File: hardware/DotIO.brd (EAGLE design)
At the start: 30 x 65 mm, 37 parts, among them CN1 1X4-BIG, U1 ATMEGA328P-MU-QFN32, X1 S4B-ZR, X2 S4B-ZR, X3 S4B-ZR, X4 S4B-ZR, X5 S4B-ZR, X6 S4B-ZR, X7 S4B-ZR

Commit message: Initial routing
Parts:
- removed LED5, LED6, LED7, LED8: (no value), SparkFun:LED-0603
- removed X2: S4B-ZR, con-jst:S4B-ZR
- added C1, C9: 1uF, rcl:C0603
- added D1, D2: (no value), diode:SOD523
- added IC2: (no value), MCP1700:SOT-23
- added J3: USB-MICROB, SparkFun-Retired:USB-MICROB
- added R6: 68Ω, rcl:R0603
- added R8: 1.5kΩ, rcl:R0603
- R2: value 150Ω -> 68Ω; device SparkFun:0603-ARV -> rcl:R0603
- moved CN1 67.2 mm to (9.30, 28.0), turned to 0 degrees
- moved R2 47.5 mm to (8.12, 7.39), turned to 0 degrees
- moved LED2 45.9 mm to (2.06, 48.1), turned to 180 degrees
- moved LOGO1 17.0 mm to (2.50, 28.8), turned to 90 degrees
- moved R7 16.2 mm to (2.37, 17.3)
- moved C2 13.8 mm to (2.73, 52.8), turned to 270 degrees
- moved R4 11.2 mm to (21.4, 54.1), turned to 270 degrees
- moved U1 4.90 mm to (13.5, 16.2)
- moved Y1 4.76 mm to (14.7, 10.9)
- moved X1 1.62 mm to (5.06, 60.6), flipped to the bottom, turned to 90 degrees
- moved R3 1.10 mm to (20.9, 28.1)
- moved LED3 0.59 mm to (21.0, 41.7)
- moved LED4 0.53 mm to (21.0, 39.6)
- moved LED12 0.43 mm to (20.9, 31.8)
- moved LED11 0.42 mm to (20.9, 34.2)
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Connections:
- net LED renamed RGB_RED
- removed net ADCENA: U1.13
- removed net CS_FLASH: U1.23
- removed net N$11: LED6.C, R2.1
- removed net N$12: LED7.C, R2.2
- removed net N$13: LED8.C, R2.4
- removed net N$3: LED5.C, R2.3
- removed net OUTA: LED11.A, LED3.A, LED5.A, LED6.A, U1.14, X1.3, X2.3, X3.3, X5.3
- removed net OUTB: LED12.A, LED4.A, LED7.A, LED8.A, X1.2, X2.2, X3.2, X5.2
- removed net RSEL: U1.26
- removed net RXD: R1.3
- removed net TXD: R1.2
- new net 4_0: LED11.A, U1.23, X5.3
- new net 4_1: LED12.A, U1.24, X5.2
- new net 5_0: LED3.A, U1.25, X3.3
- new net 5_1: LED4.A, U1.26, X3.2
- new net RGB_BLUE: R1.3, U1.14
- new net RGB_GREEN: R1.2, U1.13
- new net USB_D+: D2.C, J3.D+, R2.1
- new net USB_D-: D1.C, J3.D-, R6.1, R8.1
- net +3V3: now also C1.1, IC2.2, R8.2, X1.3
- net +5V: now also C9.1, IC2.3, J3.VBUS; no longer X1.4, X2.4
- net D+: now also R2.2; no longer U1.25
- net D-: now also R6.2; no longer U1.24
- net GND: now also C1.2, C9.2, D1.A, D2.A, IC2.1, J3.GND, J3.MT1, J3.MT2, X1.4; no longer R2.5, R2.6, R2.7, R2.8, X1.1, X2.1
- net SCL: now also X1.2
- net SDA: now also X1.1
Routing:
- net +3V3: track 0.00 -> 162.6 mm, vias 0 -> 2
- net SCL: track 0.00 -> 72.6 mm, vias 0 -> 2
- net +5V: track 0.00 -> 70.9 mm, vias 0 -> 2
- net PUSH_RIGHT: track 0.00 -> 63.1 mm, vias 0 -> 2
- net SDA: track 0.00 -> 60.6 mm, vias 0 -> 3
- net RGB_RED: track 0.00 -> 55.2 mm, vias 0 -> 4
- net RGB_GREEN: track 0.00 -> 53.7 mm, vias 0 -> 2
- net RGB_BLUE: track 0.00 -> 49.6 mm, vias 0 -> 2
- net PUSH_UP: track 0.00 -> 48.4 mm, vias 0 -> 2
- net 5_0: track 0.00 -> 45.9 mm, vias 0 -> 2
- net 2_0: track 0.00 -> 45.0 mm
- net MOSI: track 0.00 -> 38.7 mm
- net MISO: track 0.00 -> 36.5 mm
- net SCK: track 0.00 -> 35.4 mm
- net 5_1: track 0.00 -> 34.8 mm, vias 0 -> 1
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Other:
- outline, holes or cut-outs redrawn

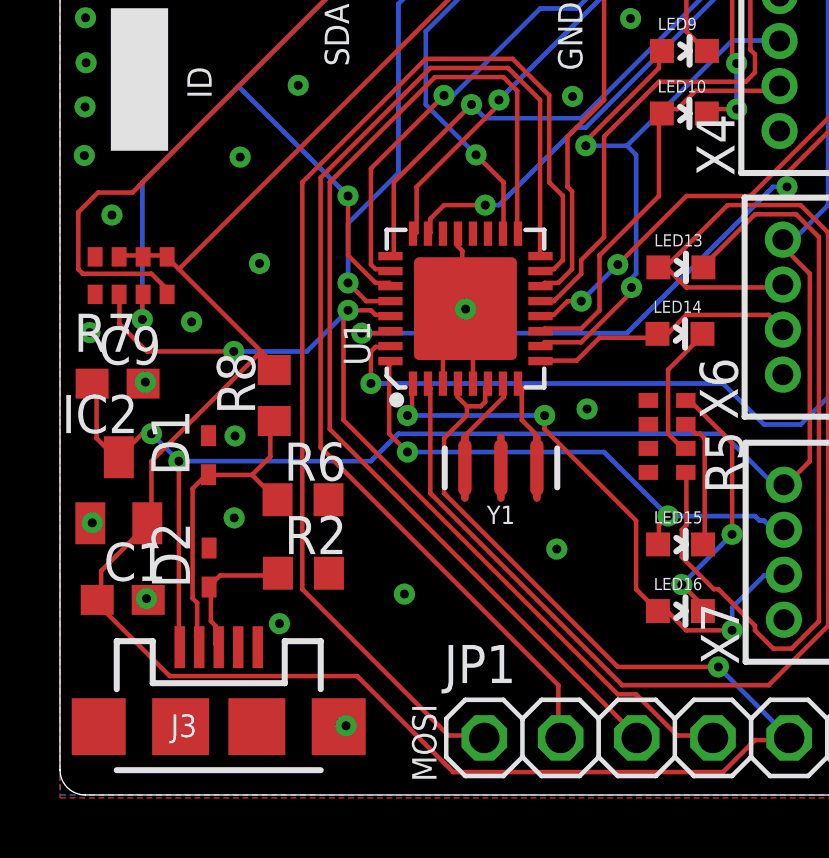
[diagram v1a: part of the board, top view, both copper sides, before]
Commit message: Bind USB to SPI pins
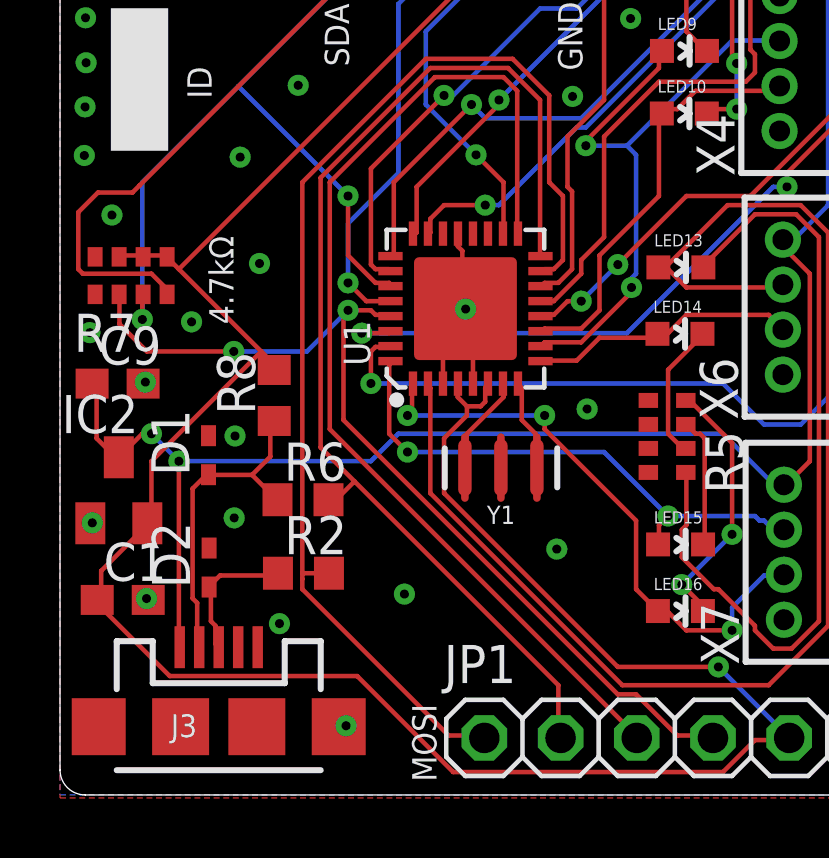
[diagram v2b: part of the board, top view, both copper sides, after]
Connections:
- removed net D+: R2.2
- removed net D-: R6.2
- net MISO: now also R6.2
- net MOSI: now also R2.2
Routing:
- net MISO: track 36.5 -> 37.6 mm
- net MOSI: track 38.7 -> 39.6 mm
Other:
- board text added: "4.7kΩ"
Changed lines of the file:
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@@
 <rectangle x1="10.73" y1="13.265" x2="16.46" y2="19.08" layer="43"/>
 <rectangle x1="0.905" y1="27.01" x2="4.305" y2="38.25" layer="43"/>
+<text x="5.785" y="15.69" size="0.8128" layer="21" rot="R90">4.7kΩ</text>
 </plain>
 <attributes>
@@
 <wire x1="12.192" y1="24.5364" x2="15.0876" y2="24.5364" width="0.1524" layer="1"/>
 <wire x1="8.0772" y1="20.4216" x2="12.192" y2="24.5364" width="0.1524" layer="1"/>
-<wire x1="8.0772" y1="6.858" x2="8.0772" y2="20.4216" width="0.1524" layer="1"/>
+<wire x1="8.0772" y1="6.858" x2="8.0772" y2="7.2" width="0.1524" layer="1"/>
+<wire x1="8.0772" y1="7.39" x2="8.0772" y2="20.4216" width="0.1524" layer="1"/>
 <wire x1="12.954" y1="1.9812" x2="8.0772" y2="6.858" width="0.1524" layer="1"/>
 <wire x1="14.0208" y1="1.9812" x2="12.954" y2="1.9812" width="0.1524" layer="1"/>
 <wire x1="16.1544" y1="17.526" x2="16.015" y2="17.46" width="0.1524" layer="1"/>
 <wire x1="14.0208" y1="1.9812" x2="14.145" y2="1.9" width="0.1524" layer="1"/>
+<contactref element="R2" pad="2"/>
+<wire x1="8.965" y1="7.39" x2="8.0772" y2="7.39" width="0.1524" layer="1"/>
+<wire x1="8.0772" y1="7.39" x2="8.0772" y2="7.2" width="0.1524" layer="1"/>
 </signal>
 <signal name="MISO">
@@
 <wire x1="8.6868" y1="20.574" x2="12.3444" y2="24.2316" width="0.1524" layer="1"/>
 <wire x1="8.6868" y1="11.5824" x2="8.6868" y2="20.574" width="0.1524" layer="1"/>
-<wire x1="16.6116" y1="3.6576" x2="8.6868" y2="11.5824" width="0.1524" layer="1"/>
+<wire x1="16.6116" y1="3.6576" x2="9.8171" y2="10.4521" width="0.1524" layer="1"/>
+<wire x1="9.8171" y1="10.4521" x2="8.6868" y2="11.5824" width="0.1524" layer="1"/>
 <wire x1="16.6116" y1="1.9812" x2="16.6116" y2="3.6576" width="0.1524" layer="1"/>
 <wire x1="16.002" y1="17.9832" x2="16.015" y2="17.96" width="0.1524" layer="1"/>
 <wire x1="16.6116" y1="1.9812" x2="16.685" y2="1.9" width="0.1524" layer="1"/>
+<contactref element="R6" pad="2"/>
+<wire x1="8.95" y1="9.84" x2="9.205" y2="9.84" width="0.1524" layer="1"/>
+<wire x1="9.205" y1="9.84" x2="9.8171" y2="10.4521" width="0.1524" layer="1"/>
 </signal>
 <signal name="SCK">
@@
 <wire x1="5.0292" y1="7.0104" x2="4.97" y2="6.93" width="0.1524" layer="1"/>
 </signal>
-<signal name="D-">
-<contactref element="R6" pad="2"/>
-</signal>
-<signal name="D+">
-<contactref element="R2" pad="2"/>
-</signal>
 <signal name="RGB_RED">

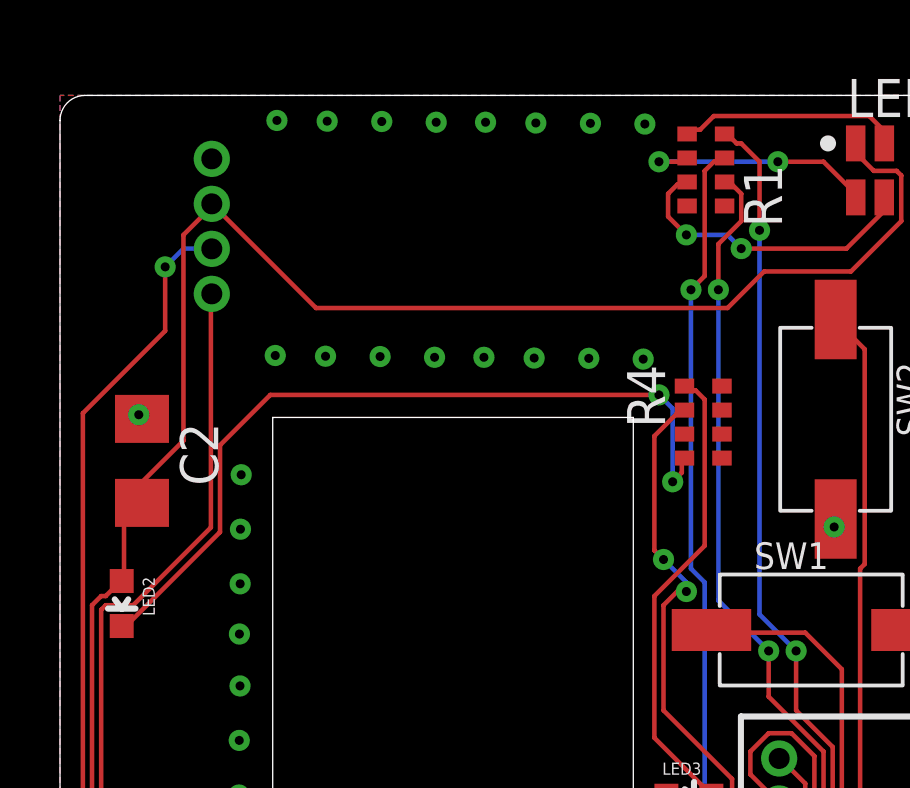
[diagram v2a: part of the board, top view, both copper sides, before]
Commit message: Flip I2C JST port
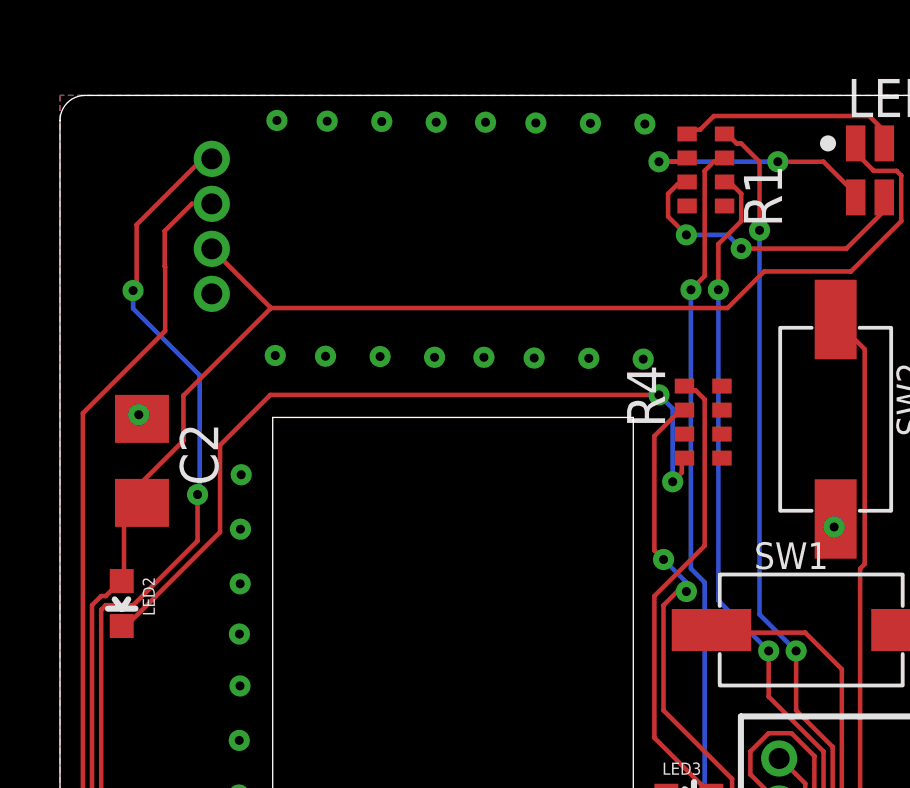
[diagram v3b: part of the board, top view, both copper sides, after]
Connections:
- net +3V3: now also X1.2; no longer X1.3
- net GND: now also X1.1; no longer X1.4
- net SCL: now also X1.3; no longer X1.2
- net SDA: now also X1.4; no longer X1.1
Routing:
- net SDA: track 60.6 -> 67.1 mm, vias 3 -> 5
- net +3V3: track 162.6 -> 159.3 mm
- net SCL: track 72.6 -> 74.0 mm, vias 2 -> 1
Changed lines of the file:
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@@
 <contactref element="J3" pad="MT1"/>
 <contactref element="J3" pad="GND"/>
-<contactref element="X1" pad="4"/>
 <wire x1="13.4112" y1="18.1356" x2="13.4112" y2="16.3068" width="0.1524" layer="1"/>
 <wire x1="13.2588" y1="18.288" x2="13.4112" y2="18.1356" width="0.1524" layer="1"/>
@@
 <via x="21.565" y="28.445" extent="1-16" drill="0.3"/>
 <via x="17.085" y="23.285" extent="1-16" drill="0.3"/>
+<contactref element="X1" pad="1"/>
 <wire x1="21.505" y1="28.465" x2="21.565" y2="28.445" width="0" layer="19" extent="1-1"/>
 <wire x1="2.77" y1="13.71" x2="2.845" y2="13.76" width="0" layer="19" extent="1-1"/>
@@
 <contactref element="R7" pad="3"/>
 <contactref element="CN1" pad="1"/>
-<contactref element="X1" pad="1"/>
 <wire x1="2.7432" y1="15.8496" x2="2.7432" y2="16.6116" width="0.1524" layer="1"/>
 <wire x1="2.7432" y1="20.4216" x2="2.7432" y2="15.8496" width="0.1524" layer="16"/>
@@
 <wire x1="5.9436" y1="23.622" x2="9.6012" y2="19.9644" width="0.1524" layer="16"/>
 <wire x1="10.9728" y1="17.0688" x2="11.015" y2="16.96" width="0.1524" layer="1"/>
-<wire x1="5.0292" y1="50.5968" x2="5.0292" y2="58.3692" width="0.1524" layer="1"/>
-<wire x1="2.4384" y1="48.006" x2="5.0292" y2="50.5968" width="0.1524" layer="1"/>
 <wire x1="1.524" y1="48.006" x2="2.4384" y2="48.006" width="0.1524" layer="1"/>
 <wire x1="1.3716" y1="47.8536" x2="1.524" y2="48.006" width="0.1524" layer="1"/>
@@
 <wire x1="9.2964" y1="28.3464" x2="5.9436" y2="31.6992" width="0.1524" layer="16"/>
 <wire x1="9.2964" y1="28.0416" x2="9.2964" y2="28.3464" width="0.1524" layer="16"/>
-<wire x1="5.0292" y1="58.3692" x2="5.06" y2="58.385" width="0.1524" layer="1"/>
 <wire x1="9.2964" y1="28.0416" x2="9.3028" y2="28.019" width="0.1524" layer="16"/>
 <via x="2.7432" y="15.8496" extent="1-16" drill="0.3"/>
 <via x="9.6012" y="19.9644" extent="1-16" drill="0.3"/>
 <via x="6.096" y="33.3756" extent="1-16" drill="0.3"/>
+<contactref element="X1" pad="4"/>
+<wire x1="5.06" y1="62.885" x2="4.75" y2="62.885" width="0.1524" layer="1"/>
+<wire x1="4.75" y1="62.885" x2="2.555" y2="60.69" width="0.1524" layer="1"/>
+<wire x1="2.555" y1="60.69" x2="2.555" y2="58.615" width="0.1524" layer="1"/>
+<wire x1="2.555" y1="58.615" x2="2.435" y2="58.495" width="0.1524" layer="1"/>
+<via x="2.435" y="58.495" extent="1-16" drill="0.3"/>
+<wire x1="2.435" y1="58.495" x2="2.435" y2="57.895" width="0.1524" layer="16"/>
+<wire x1="2.435" y1="57.895" x2="4.655" y2="55.675" width="0.1524" layer="16"/>
+<wire x1="4.655" y1="55.675" x2="4.655" y2="51.765" width="0.1524" layer="16"/>
+<wire x1="4.655" y1="51.765" x2="4.585" y2="51.695" width="0.1524" layer="16"/>
+<via x="4.585" y="51.695" extent="1-16" drill="0.3"/>
+<wire x1="4.585" y1="51.695" x2="4.585" y2="50.1526" width="0.1524" layer="1"/>
+<wire x1="4.585" y1="50.1526" x2="2.4384" y2="48.006" width="0.1524" layer="1"/>
 </signal>
 <signal name="RST">
@@
 <contactref element="IC2" pad="2"/>
 <contactref element="R8" pad="2"/>
-<contactref element="X1" pad="3"/>
 <wire x1="2.1336" y1="50.9016" x2="2.1336" y2="48.9204" width="0.1524" layer="1"/>
 <wire x1="2.5908" y1="51.3588" x2="2.1336" y2="50.9016" width="0.1524" layer="1"/>
@@
 <wire x1="23.4696" y1="59.1312" x2="26.3652" y2="59.1312" width="0.1524" layer="1"/>
 <wire x1="22.2504" y1="57.912" x2="23.4696" y2="59.1312" width="0.1524" layer="1"/>
-<wire x1="8.5344" y1="57.912" x2="22.2504" y2="57.912" width="0.1524" layer="1"/>
-<wire x1="5.1816" y1="61.2648" x2="8.5344" y2="57.912" width="0.1524" layer="1"/>
+<wire x1="7.033" y1="57.912" x2="22.2504" y2="57.912" width="0.1524" layer="1"/>
 <wire x1="26.67" y1="63.3984" x2="26.5225" y2="63.4" width="0.1524" layer="1"/>
-<wire x1="5.1816" y1="61.2648" x2="5.06" y2="61.385" width="0.1524" layer="1"/>
 <wire x1="2.7432" y1="52.1208" x2="2.7432" y2="51.5112" width="0.1524" layer="1"/>
 <wire x1="4.1148" y1="53.4924" x2="2.7432" y2="52.1208" width="0.1524" layer="1"/>
-<wire x1="4.1148" y1="60.3504" x2="4.1148" y2="53.4924" width="0.1524" layer="1"/>
-<wire x1="5.0292" y1="61.2648" x2="4.1148" y2="60.3504" width="0.1524" layer="1"/>
 <wire x1="2.7432" y1="51.5112" x2="2.732284375" y2="51.417190625" width="0.1524" layer="1"/>
-<wire x1="5.0292" y1="61.2648" x2="5.06" y2="61.385" width="0.1524" layer="1"/>
 <wire x1="13.2588" y1="13.2588" x2="13.2588" y2="13.5636" width="0.1524" layer="1"/>
 <wire x1="13.5636" y1="12.954" x2="13.2588" y2="13.2588" width="0.1524" layer="1"/>
@@
 <via x="21.9456" y="4.2672" extent="1-16" drill="0.3"/>
 <via x="13.8684" y="21.336" extent="1-16" drill="0.3"/>
+<contactref element="X1" pad="2"/>
+<wire x1="7.033" y1="57.912" x2="5.06" y2="59.885" width="0.1524" layer="1"/>
+<wire x1="4.1148" y1="53.4924" x2="4.1148" y2="54.9938" width="0.1524" layer="1"/>
+<wire x1="4.1148" y1="54.9938" x2="7.033" y2="57.912" width="0.1524" layer="1"/>
 </signal>
 <signal name="MOSI">
@@
 <contactref element="R7" pad="4"/>
 <contactref element="CN1" pad="2"/>
-<contactref element="X1" pad="2"/>
 <wire x1="3.5052" y1="16.9164" x2="3.5052" y2="16.764" width="0.1524" layer="1"/>
 <wire x1="3.048" y1="17.3736" x2="3.5052" y2="16.9164" width="0.1524" layer="1"/>
@@
 <wire x1="10.9728" y1="16.4592" x2="11.015" y2="16.46" width="0.1524" layer="1"/>
 <wire x1="11.7348" y1="27.8892" x2="11.8428" y2="28.019" width="0.1524" layer="16"/>
-<wire x1="4.1148" y1="59.8932" x2="5.0292" y2="59.8932" width="0.1524" layer="16"/>
-<wire x1="3.5052" y1="59.2836" x2="4.1148" y2="59.8932" width="0.1524" layer="16"/>
 <wire x1="3.5052" y1="57.15" x2="3.5052" y2="59.2836" width="0.1524" layer="1"/>
 <wire x1="0.762" y1="54.4068" x2="3.5052" y2="57.15" width="0.1524" layer="1"/>
 <wire x1="0.762" y1="34.8996" x2="0.762" y2="54.4068" width="0.1524" layer="1"/>
 <wire x1="8.9916" y1="26.67" x2="0.762" y2="34.8996" width="0.1524" layer="1"/>
-<wire x1="5.0292" y1="59.8932" x2="5.06" y2="59.885" width="0.1524" layer="16"/>
 <via x="9.6012" y="17.0688" extent="1-16" drill="0.3"/>
-<via x="3.5052" y="59.2836" extent="1-16" drill="0.3"/>
+<contactref element="X1" pad="3"/>
+<wire x1="5.06" y1="61.385" x2="4.395" y2="61.385" width="0.1524" layer="1"/>
+<wire x1="4.395" y1="61.385" x2="3.49" y2="60.48" width="0.1524" layer="1"/>
+<wire x1="3.49" y1="60.48" x2="3.49" y2="59.2988" width="0.1524" layer="1"/>
+<wire x1="3.49" y1="59.2988" x2="3.5052" y2="59.2836" width="0.1524" layer="1"/>
 </signal>
 <signal name="ADC">
